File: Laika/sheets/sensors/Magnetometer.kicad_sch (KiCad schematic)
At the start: 0 parts

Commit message: Imported symbol/footprint for Memsic MMC5983MA
Imported footprint from SnapEDA for the Memsic MMC5983MA
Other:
- note added: "Magnetometer"
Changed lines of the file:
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@@
 	(generator_version "9.0")
 	(paper "A4")
+	(rectangle
+		(start 76.2 50.8)
+		(end 203.2 127)
+		(stroke
+			(width 0)
+			(type default)
+		)
+		(fill
+			(type none)
+		)
+	)
+	(text "Magnetometer"
+		(exclude_from_sim no)
+		(at 139.7 25.4 0)
+		(effects
+			(font
+				(size 6.5024 6.5024)
+				(thickness 0.254)
+				(bold yes)
+			)
+		)
+	)
+	(text "Magnetometer"
+		(exclude_from_sim no)
+		(at 76.2 127 0)
+		(effects
+			(font
+				(size 1.27 1.27)
+				(thickness 0.254)
+				(bold yes)
+			)
+			(justify left bottom)
+		)
+	)
 )

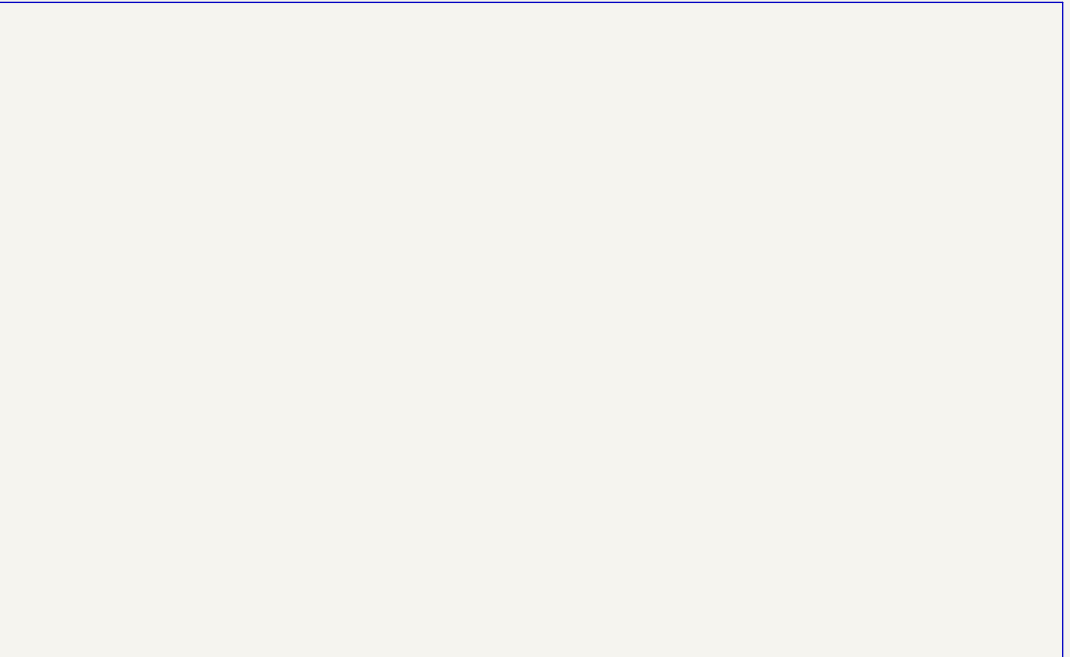
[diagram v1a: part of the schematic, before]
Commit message: Created schematic for MMC5983MA Magnetometer
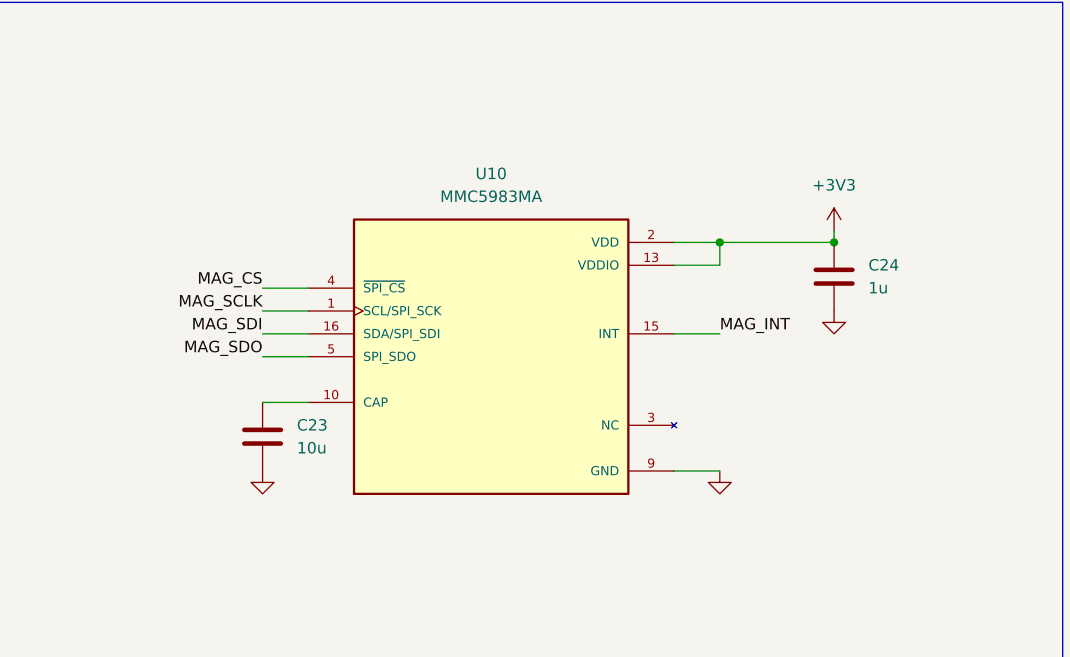
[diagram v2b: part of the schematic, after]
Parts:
- added C23: 10u, symbol Device:C
- added C24: 1u, symbol Device:C
- added U10: MMC5983MA, MMC5983MA:PQFN50P300X300X100-16N, symbol MMC5983MA:MMC5983MA
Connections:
- new net: C23.1, U10.10 (CAP)
- new net: U10.12 (NC), U10.14 (NC), U10.3 (NC), U10.6 (NC), U10.7 (NC), U10.8 (NC)
- new net +3V3: C24.1, U10.13 (VDDIO), U10.2 (VDD)
- new net GND: C23.2, C24.2, U10.11 (GND), U10.9 (GND)
- new net MAG_CS: U10.4 (~{SPI_CS})
- new net MAG_INT: U10.15 (INT)
- new net MAG_SCLK: U10.1 (SCL/SPI_SCK)
- new net MAG_SDI: U10.16 (SDA/SPI_SDI)
- new net MAG_SDO: U10.5 (SPI_SDO)

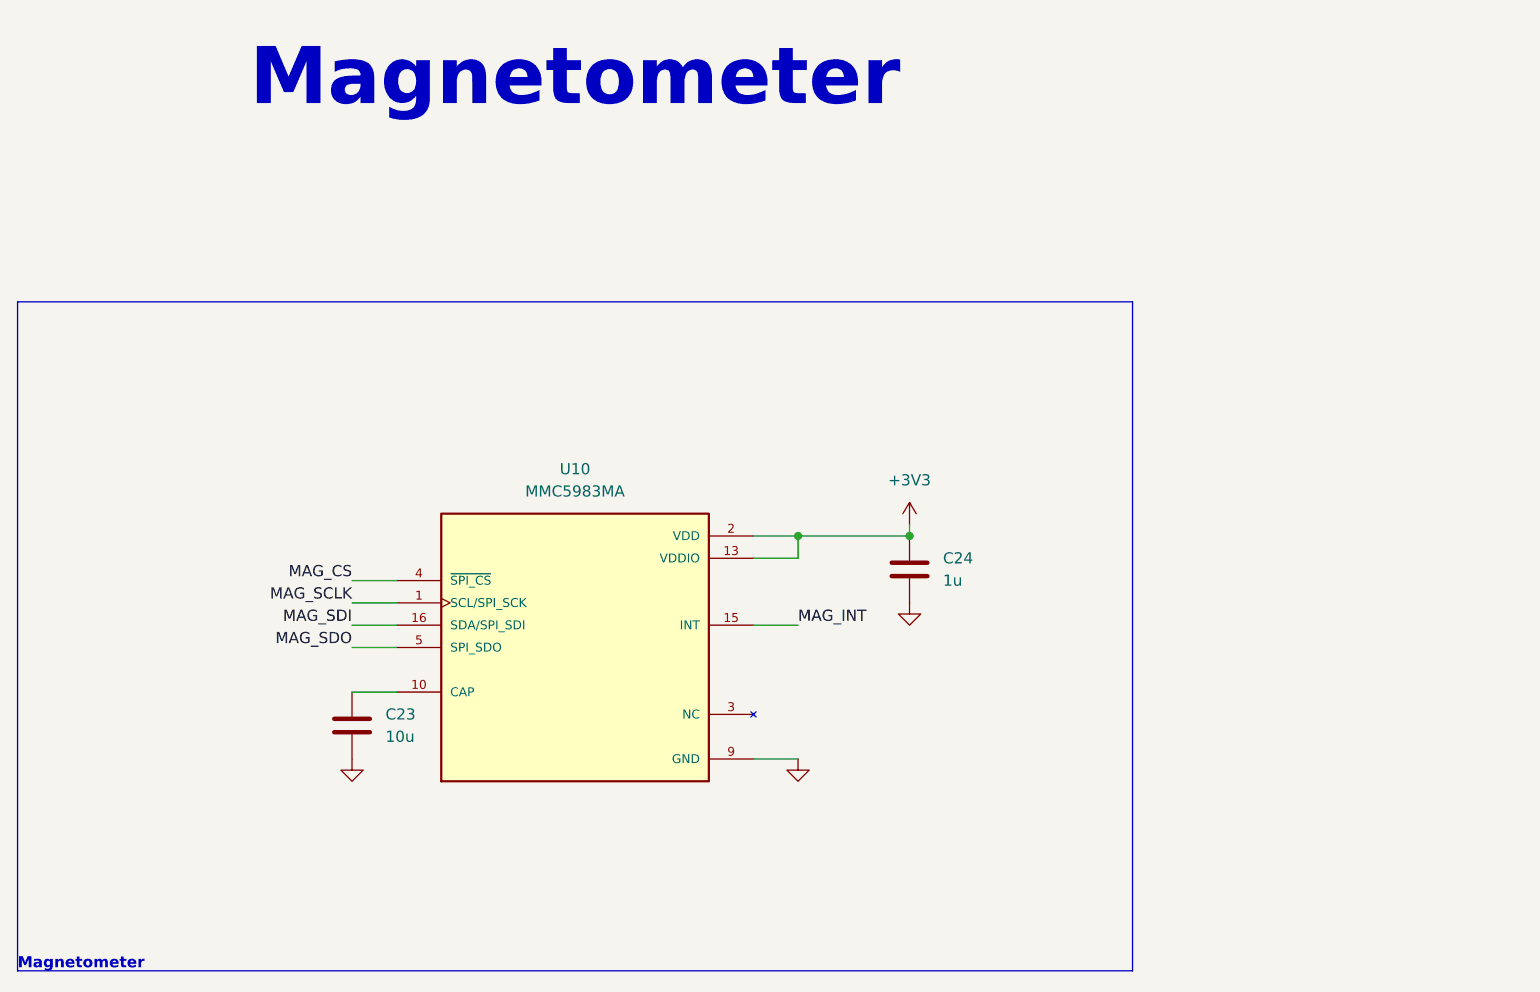
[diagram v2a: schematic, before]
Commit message: Connected sensors to SPI3
Connected Sensor Bus to SPI3. Rearranged GPS reset, pps, and buzzer pins
to other 3.3V logic pins. Connected SPI chip selects. Deleted interrupt
bus from sensors due to lack of 3.3V pins.
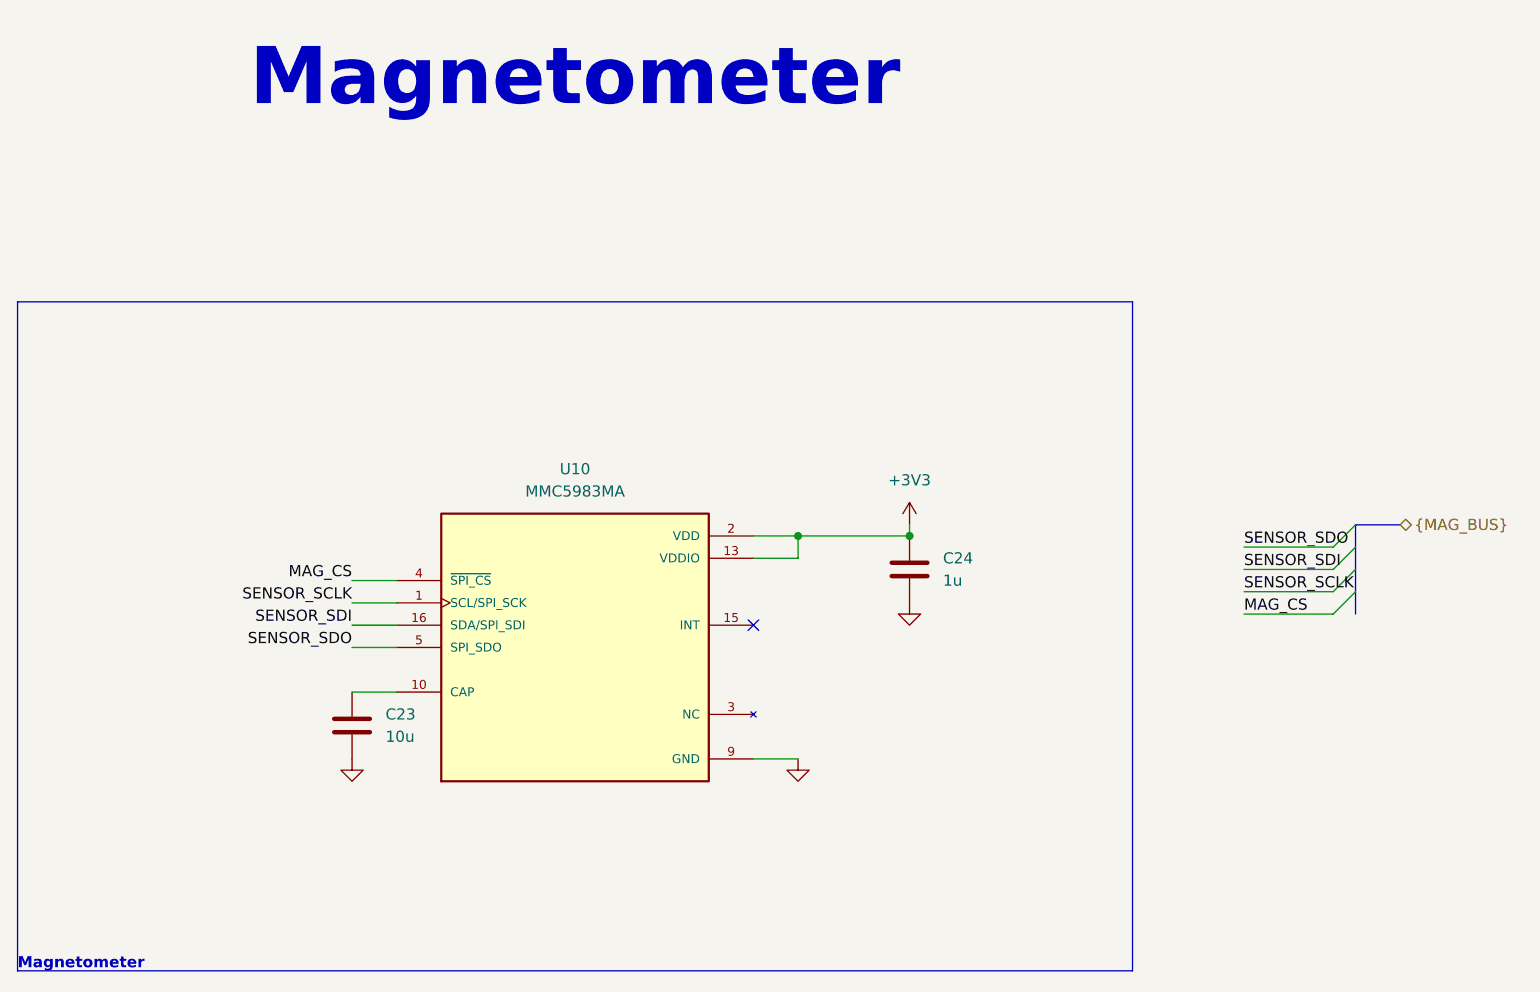
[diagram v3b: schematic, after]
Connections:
- net MAG_INT: no longer names the net of U10.15 (INT)
- net MAG_SCLK renamed SENSOR_SCLK
- net MAG_SDI renamed SENSOR_SDI
- net MAG_SDO renamed SENSOR_SDO
- no-connect marks 0 -> 1
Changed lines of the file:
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@@
 	(generator_version "9.0")
 	(paper "A4")
+	(bus_alias "MAG_BUS"
+		(members "SENSOR_SDO" "SENSOR_SDI" "SENSOR_SCLK" "MAG_CS")
+	)
 	(rectangle
 		(start 76.2 50.8)
@@
 		(color 0 0 0 0)
 	)
+	(no_connect
+		(at 160.02 87.63)
+	)
+	(bus_entry
+		(at 228.6 83.82)
+		(size -2.54 2.54)
+		(stroke
+			(width 0)
+			(type default)
+		)
+	)
+	(bus_entry
+		(at 228.6 81.28)
+		(size -2.54 2.54)
+		(stroke
+			(width 0)
+			(type default)
+		)
+	)
+	(bus_entry
+		(at 228.6 78.74)
+		(size -2.54 2.54)
+		(stroke
+			(width 0)
+			(type default)
+		)
+	)
+	(bus_entry
+		(at 228.6 76.2)
+		(size -2.54 2.54)
+		(stroke
+			(width 0)
+			(type default)
+		)
+	)
 	(wire
 		(pts
@@
 	(wire
 		(pts
+			(xy 215.9 78.74) (xy 226.06 78.74)
+		)
+		(stroke
+			(width 0)
+			(type default)
+		)
+	)
+	(wire
+		(pts
 			(xy 160.02 77.47) (xy 165.1 77.47)
 		)
@@
 		)
 	)
+	(bus
+		(pts
+			(xy 228.6 76.2) (xy 228.6 78.74)
+		)
+		(stroke
+			(width 0)
+			(type default)
+		)
+	)
 	(wire
 		(pts
@@
 	(wire
 		(pts
+			(xy 215.9 83.82) (xy 226.06 83.82)
+		)
+		(stroke
+			(width 0)
+			(type default)
+		)
+	)
+	(wire
+		(pts
+			(xy 215.9 81.28) (xy 226.06 81.28)
+		)
+		(stroke
+			(width 0)
+			(type default)
+		)
+	)
+	(wire
+		(pts
 			(xy 165.1 102.87) (xy 160.02 102.87)
 		)
@@
 		)
 	)
-	(wire
-		(pts
-			(xy 165.1 87.63) (xy 160.02 87.63)
+	(bus
+		(pts
+			(xy 228.6 78.74) (xy 228.6 81.28)
+		)
+		(stroke
+			(width 0)
+			(type default)
+		)
+	)
+	(bus
+		(pts
+			(xy 228.6 83.82) (xy 228.6 86.36)
+		)
+		(stroke
+			(width 0)
+			(type default)
+		)
+	)
+	(bus
+		(pts
+			(xy 233.68 76.2) (xy 228.6 76.2)
+		)
+		(stroke
+			(width 0)
+			(type default)
+		)
+	)
+	(wire
+		(pts
+			(xy 215.9 86.36) (xy 226.06 86.36)
+		)
+		(stroke
+			(width 0)
+			(type default)
+		)
+	)
+	(bus
+		(pts
+			(xy 228.6 81.28) (xy 228.6 83.82)
 		)
 		(stroke
@@
 		)
 	)
-	(label "MAG_SDI"
+	(label "SENSOR_SDI"
 		(at 114.3 87.63 180)
 		(effects
@@
 		)
 	)
-	(label "MAG_SCLK"
+	(label "MAG_CS"
+		(at 215.9 86.36 0)
+		(effects
+			(font
+				(size 1.27 1.27)
+			)
+			(justify left bottom)
+		)
+	)
+	(label "SENSOR_SDO"
+		(at 215.9 78.74 0)
+		(effects
+			(font
+				(size 1.27 1.27)
+			)
+			(justify left bottom)
+		)
+	)
+	(label "SENSOR_SCLK"
 		(at 114.3 85.09 180)
 		(effects
@@
 		)
 	)
-	(label "MAG_SDO"
+	(label "SENSOR_SDO"
 		(at 114.3 90.17 180)
 		(effects
@@
 		)
 	)
-	(label "MAG_INT"
-		(at 165.1 87.63 0)
+	(label "SENSOR_SCLK"
+		(at 215.9 83.82 0)
+		(effects
+			(font
+				(size 1.27 1.27)
+			)
+			(justify left bottom)
+		)
+	)
+	(label "SENSOR_SDI"
+		(at 215.9 81.28 0)
 		(effects
 			(font
@@
 		)
 	)
+	(hierarchical_label "{MAG_BUS}"
+		(shape bidirectional)
+		(at 233.68 76.2 0)
+		(effects
+			(font
+				(size 1.27 1.27)
+			)
+			(justify left)
+		)
+	)

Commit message: Populated BOM with part numbers and footprints
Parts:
- C23: footprint (none) -> Capacitor_SMD:C_0402_1005Metric; JLC Part Type (none) -> Basic; Manafacturer (none) -> Samsung Electro-Mechanics; Part Number (none) -> CL05A106MQ5NUNC
- C24: footprint (none) -> Capacitor_SMD:C_0402_1005Metric; JLC Part Type (none) -> Basic; Manafacturer (none) -> Samsung Electro-Mechanics; Part Number (none) -> CL05A105KA5NQNC
- U10: JLC Part Type (none) -> Extended; Manafacturer (none) -> Memsic Inc.; Part Number (none) -> MMC5983MA
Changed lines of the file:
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@@
 			)
 		)
-		(property "Footprint" ""
+		(property "Footprint" "Capacitor_SMD:C_0402_1005Metric"
 			(at 115.2652 102.87 0)
 			(effects
@@
 			)
 		)
-		(property "Datasheet" "~"
+		(property "Datasheet" "https://www.samsungsem.com/resources/file/global/support/product_catalog/MLCC.pdf"
 			(at 114.3 99.06 0)
 			(effects
@@
 		)
 		(property "Description" "Unpolarized capacitor"
+			(at 114.3 99.06 0)
+			(effects
+				(font
+					(size 1.27 1.27)
+				)
+				(hide yes)
+			)
+		)
+		(property "JLC Part Type" "Basic"
+			(at 114.3 99.06 0)
+			(effects
+				(font
+					(size 1.27 1.27)
+				)
+				(hide yes)
+			)
+		)
+		(property "Manafacturer" "Samsung Electro-Mechanics"
+			(at 114.3 99.06 0)
+			(effects
+				(font
+					(size 1.27 1.27)
+				)
+				(hide yes)
+			)
+		)
+		(property "Part Number" "CL05A106MQ5NUNC"
 			(at 114.3 99.06 0)
 			(effects
@@
 			)
 		)
-		(property "Footprint" ""
+		(property "Footprint" "Capacitor_SMD:C_0402_1005Metric"
 			(at 178.7652 85.09 0)
 			(effects
@@
 			)
 		)
-		(property "Datasheet" "~"
+		(property "Datasheet" "https://www.samsungsem.com/resources/file/global/support/product_catalog/MLCC.pdf"
 			(at 177.8 81.28 0)
 			(effects
@@
 		)
 		(property "Description" "Unpolarized capacitor"
+			(at 177.8 81.28 0)
+			(effects
+				(font
+					(size 1.27 1.27)
+				)
+				(hide yes)
+			)
+		)
+		(property "JLC Part Type" "Basic"
+			(at 177.8 81.28 0)
+			(effects
+				(font
+					(size 1.27 1.27)
+				)
+				(hide yes)
+			)
+		)
+		(property "Manafacturer" "Samsung Electro-Mechanics"
+			(at 177.8 81.28 0)
+			(effects
+				(font
+					(size 1.27 1.27)
+				)
+				(hide yes)
+			)
+		)
+		(property "Part Number" "CL05A105KA5NQNC"
 			(at 177.8 81.28 0)
 			(effects
@@
 				(hide yes)
 			)
+		)
+		(property "JLC Part Type" "Extended"
+			(at 139.7 90.17 0)
+			(effects
+				(font
+					(size 1.27 1.27)
+				)
+				(hide yes)
+			)
+		)
+		(property "Manafacturer" "Memsic Inc."
+			(at 139.7 90.17 0)
+			(effects
+				(font
+					(size 1.27 1.27)
+				)
+				(hide yes)
+			)
+		)
+		(property "Part Number" "MMC5983MA"
+			(at 139.7 90.17 0)
+			(effects
+				(font
+					(size 1.27 1.27)
+				)
+				(hide yes)
+			)
